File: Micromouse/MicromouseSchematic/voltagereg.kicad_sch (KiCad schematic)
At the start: 5 parts

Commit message: added resistors, must need to add capacitors
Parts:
- C2: footprint Capacitor_SMD:C_0603_1608Metric -> (none)
- Cin_VR1: footprint Capacitor_SMD:C_0805_2012Metric -> (none)
- Renb1, Rent1: footprint (none) -> Resistor_SMD:R_0603_1608Metric
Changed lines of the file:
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@@
 			)
 		)
-		(property "Footprint" "Capacitor_SMD:C_0603_1608Metric"
+		(property "Footprint" ""
 			(at 171.1452 97.79 0)
 			(effects
@@
 			)
 		)
-		(property "Footprint" "Capacitor_SMD:C_0805_2012Metric"
+		(property "Footprint" ""
 			(at 84.7852 101.6 0)
 			(effects
@@
 			)
 		)
-		(property "Footprint" ""
+		(property "Footprint" "Resistor_SMD:R_0603_1608Metric"
 			(at 104.902 93.98 90)
 			(effects
@@
 			)
 		)
-		(property "Footprint" ""
+		(property "Footprint" "Resistor_SMD:R_0603_1608Metric"
 			(at 104.902 102.87 90)
 			(effects

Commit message: Changd IR sensors and emmiters to 5mm LEDs
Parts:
- C2, Cin_VR1: footprint (none) -> Capacitor_SMD:C_0402_1005Metric
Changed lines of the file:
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@@
 			)
 		)
-		(property "Footprint" ""
+		(property "Footprint" "Capacitor_SMD:C_0402_1005Metric"
 			(at 171.1452 97.79 0)
 			(effects
@@
 			)
 		)
-		(property "Footprint" ""
+		(property "Footprint" "Capacitor_SMD:C_0402_1005Metric"
 			(at 84.7852 101.6 0)
 			(effects

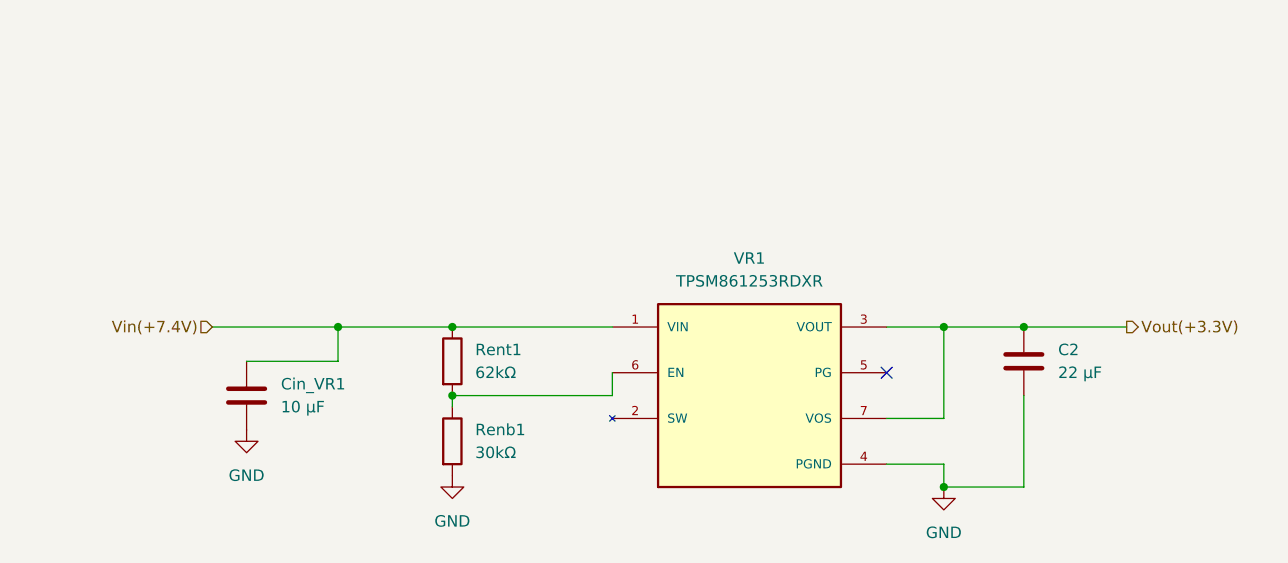
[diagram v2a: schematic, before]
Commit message: Schematics clear, moved all footprints to pcb and voltage regulator completed. The layout begins
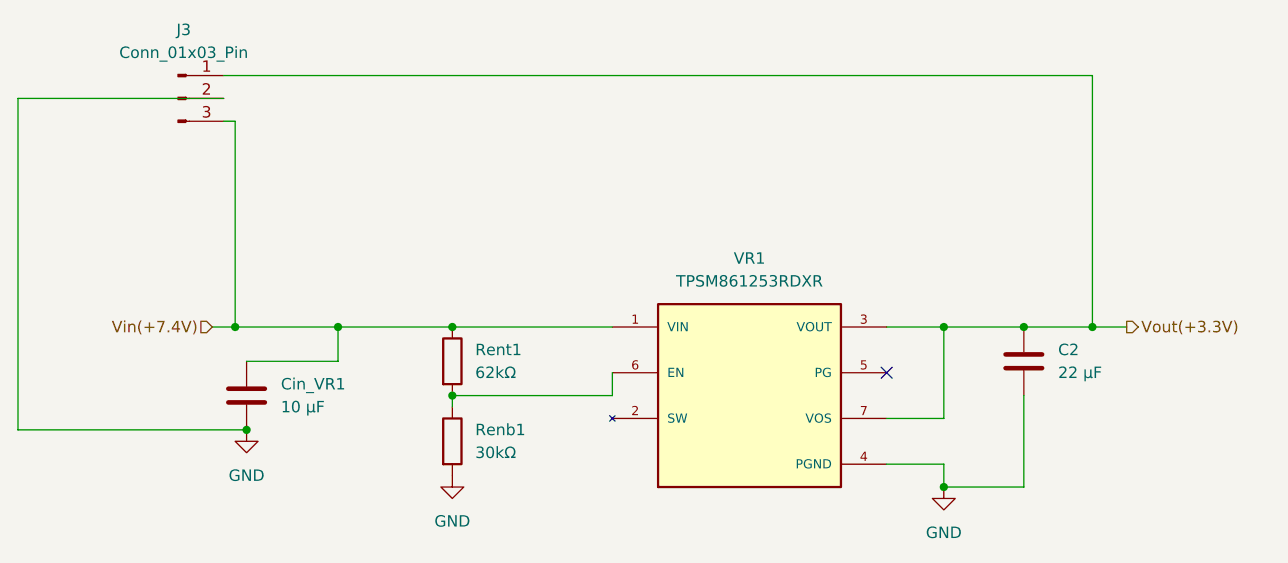
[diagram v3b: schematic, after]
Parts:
- added J3: Conn_01x03_Pin, Connector_JST:JST_PH_B3B-PH-K_1x03_P2.00mm_Vertical, symbol Connector:Conn_01x03_Pin
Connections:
- net GND: now also J3.2 (Pin_2)
- net Vin(+7.4V): now also J3.3 (Pin_3)
- net Vout(+3.3V): now also J3.1 (Pin_1)
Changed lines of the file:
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@@
 	(paper "A4")
 	(junction
+		(at 83.82 101.6)
+		(diameter 0)
+		(color 0 0 0 0)
+	)
+	(junction
 		(at 161.29 107.95)
 		(diameter 0)
@@
 	)
 	(junction
+		(at 82.55 90.17)
+		(diameter 0)
+		(color 0 0 0 0)
+	)
+	(junction
 		(at 93.98 90.17)
+		(diameter 0)
+		(color 0 0 0 0)
+	)
+	(junction
+		(at 177.8 90.17)
 		(diameter 0)
 		(color 0 0 0 0)
@@
 	(wire
 		(pts
-			(xy 80.01 90.17) (xy 93.98 90.17)
+			(xy 80.01 90.17) (xy 82.55 90.17)
 		)
 		(stroke
@@
 	(wire
 		(pts
-			(xy 170.18 90.17) (xy 181.61 90.17)
+			(xy 82.55 67.31) (xy 81.28 67.31)
+		)
+		(stroke
+			(width 0)
+			(type default)
+		)
+	)
+	(wire
+		(pts
+			(xy 170.18 90.17) (xy 177.8 90.17)
 		)
 		(stroke
@@
 	(wire
 		(pts
+			(xy 83.82 101.6) (xy 58.42 101.6)
+		)
+		(stroke
+			(width 0)
+			(type default)
+		)
+	)
+	(wire
+		(pts
+			(xy 177.8 62.23) (xy 177.8 90.17)
+		)
+		(stroke
+			(width 0)
+			(type default)
+		)
+	)
+	(wire
+		(pts
 			(xy 124.46 97.79) (xy 106.68 97.79)
 		)
@@
 	(wire
 		(pts
+			(xy 82.55 90.17) (xy 93.98 90.17)
+		)
+		(stroke
+			(width 0)
+			(type default)
+		)
+	)
+	(wire
+		(pts
+			(xy 58.42 64.77) (xy 81.28 64.77)
+		)
+		(stroke
+			(width 0)
+			(type default)
+		)
+	)
+	(wire
+		(pts
+			(xy 82.55 90.17) (xy 82.55 67.31)
+		)
+		(stroke
+			(width 0)
+			(type default)
+		)
+	)
+	(wire
+		(pts
 			(xy 170.18 107.95) (xy 161.29 107.95)
 		)
@@
 	(wire
 		(pts
+			(xy 58.42 101.6) (xy 58.42 64.77)
+		)
+		(stroke
+			(width 0)
+			(type default)
+		)
+	)
+	(wire
+		(pts
 			(xy 161.29 100.33) (xy 161.29 90.17)
 		)
@@
 		(pts
 			(xy 161.29 90.17) (xy 170.18 90.17)
+		)
+		(stroke
+			(width 0)
+			(type default)
+		)
+	)
+	(wire
+		(pts
+			(xy 177.8 90.17) (xy 181.61 90.17)
+		)
+		(stroke
+			(width 0)
+			(type default)
+		)
+	)
+	(wire
+		(pts
+			(xy 81.28 62.23) (xy 177.8 62.23)
 		)
 		(stroke
@@
 		)
 	)
+	(symbol
+		(lib_id "Connector:Conn_01x03_Pin")
+		(at 76.2 64.77 0)
+		(unit 1)
+		(exclude_from_sim no)
+		(in_bom yes)
+		(on_board yes)
+		(dnp no)
+		(fields_autoplaced yes)
+		(property "Reference" "J3"
+			(at 76.835 57.15 0)
+			(effects
+				(font
+					(size 1.27 1.27)
+				)
+			)
+		)
+		(property "Value" "Conn_01x03_Pin"
+			(at 76.835 59.69 0)
+			(effects
+				(font
+					(size 1.27 1.27)
+				)
+			)
+		)
+		(property "Footprint" "Connector_JST:JST_PH_B3B-PH-K_1x03_P2.00mm_Vertical"
+			(at 76.2 64.77 0)
+			(effects
+				(font
+					(size 1.27 1.27)
+				)
+				(hide yes)
+			)
+		)
+		(property "Datasheet" "~"
+			(at 76.2 64.77 0)
+			(effects
+				(font
+					(size 1.27 1.27)
+				)
+				(hide yes)
+			)
+		)
+		(property "Description" "Generic connector, single row, 01x03, script generated"
+			(at 76.2 64.77 0)
+			(effects
+				(font
+					(size 1.27 1.27)
+				)
+				(hide yes)
+			)
+		)
+		(pin "1"
+		)
+		(pin "2"
+		)
+		(pin "3"
+		)
+		(instances
+			(project ""
+				(path "/0dcfab91-6b00-43c0-ac0b-8c301cb559e5/3cd5e638-0450-45f9-91e1-d72f396e0d78"
+					(reference "J3")
+					(unit 1)
+				)
+			)
+		)
+	)

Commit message: to-do IMU+Mag figure it out or mutli layer pcb?
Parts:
- J3: footprint Connector_JST:JST_PH_B3B-PH-K_1x03_P2.00mm_Vertical -> Connector_JST:JST_ZH_B3B-ZR_1x03_P1.50mm_Vertical
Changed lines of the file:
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@@
 			)
 		)
-		(property "Footprint" "Connector_JST:JST_PH_B3B-PH-K_1x03_P2.00mm_Vertical"
+		(property "Footprint" "Connector_JST:JST_ZH_B3B-ZR_1x03_P1.50mm_Vertical"
 			(at 76.2 64.77 0)
 			(effects
